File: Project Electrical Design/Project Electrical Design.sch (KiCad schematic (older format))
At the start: 2 parts

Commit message: Added Adafruit 8x8 Matrix to Kicad Project
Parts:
- added A?: Adafruit_8x8_Matrix, symbol CustomParts:Adafruit_8x8_Matrix
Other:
- moved on the sheet: A?
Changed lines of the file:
@@
 L CustomParts:MTK3339-GPS-Module A?
 U 1 1 5E668337
-P 4650 2650
-F 0 "A?" H 4300 3300 50  0000 C CNN
-F 1 "MTK3339-GPS-Module" H 4000 3400 50  0000 C CNN
-F 2 "" H 4000 3400 50  0001 C CNN
-F 3 "" H 4000 3400 50  0001 C CNN
-	1    4650 2650
+P 4300 2700
+F 0 "A?" H 3950 3250 50  0000 C CNN
+F 1 "MTK3339-GPS-Module" H 3550 3350 50  0000 C CNN
+F 2 "" H 3650 3450 50  0001 C CNN
+F 3 "" H 3650 3450 50  0001 C CNN
+	1    4300 2700
 	1    0    0    -1
 $EndComp
@@
 	1    0    0    -1
 $EndComp
+$Comp
+L CustomParts:Adafruit_8x8_Matrix A?
+U 1 1 5E66D79F
+P 6750 4500
+F 0 "A?" H 8178 4521 50  0000 L CNN
+F 1 "Adafruit_8x8_Matrix" H 8178 4430 50  0000 L CNN
+F 2 "" H 7650 5200 50  0001 C CNN
+F 3 "" H 7650 5200 50  0001 C CNN
+	1    6750 4500
+	1    0    0    -1
+$EndComp

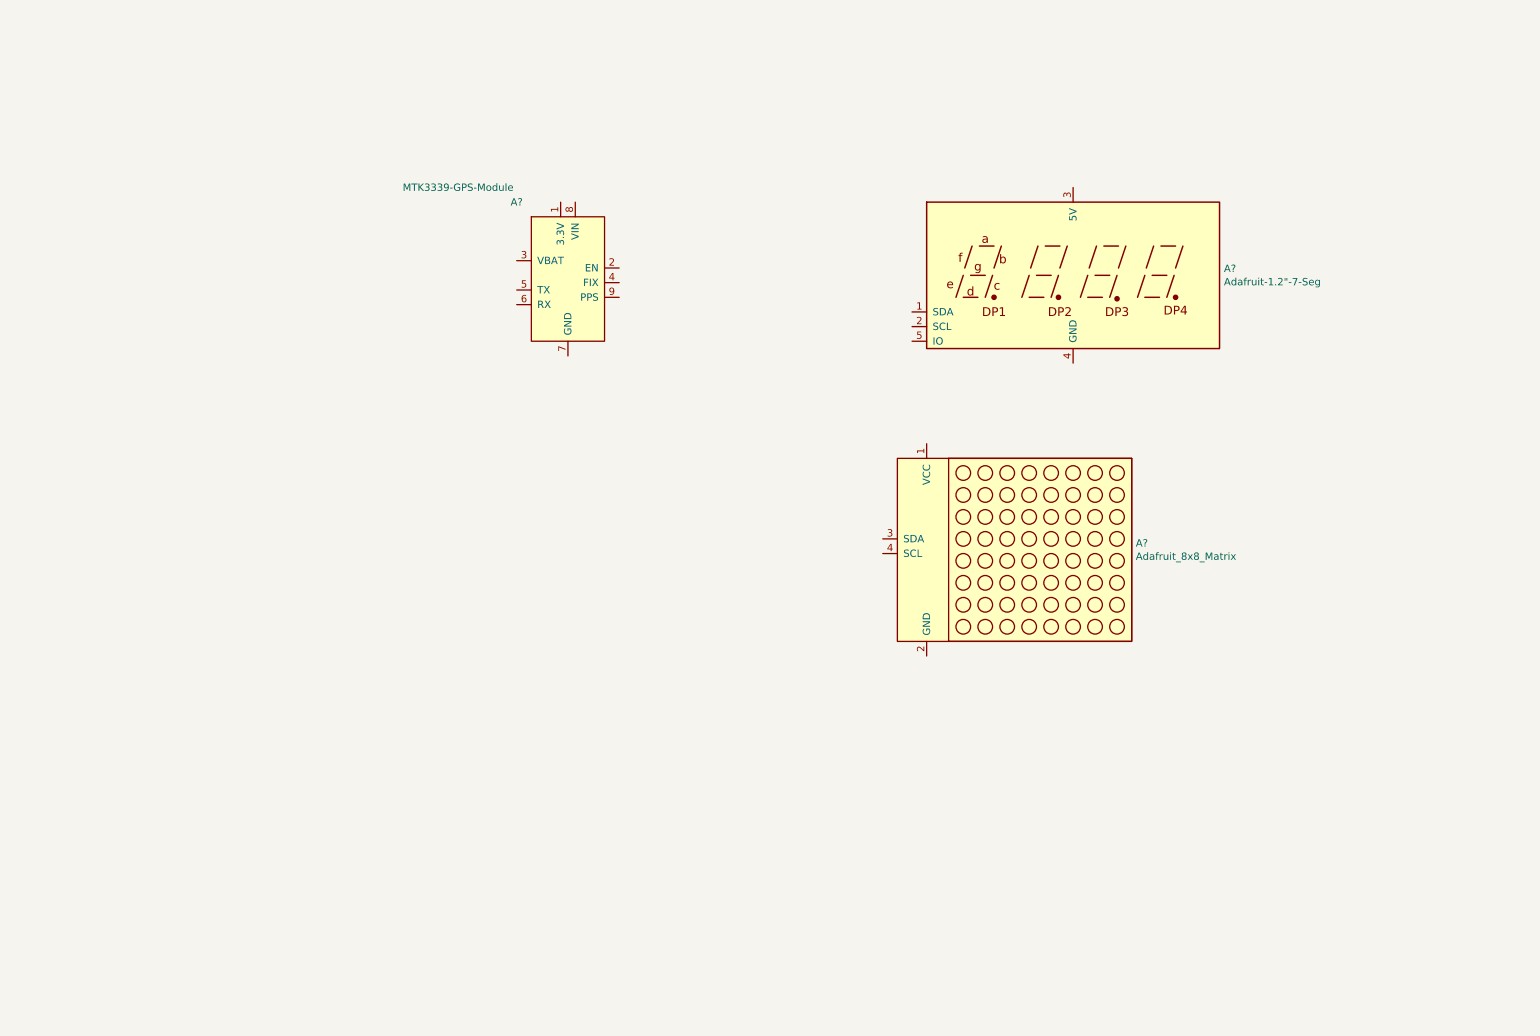
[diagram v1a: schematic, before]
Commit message: Created Component "From-Dragon-12-Board"
Please note that this component is not a complete description of the dragon 12 board.
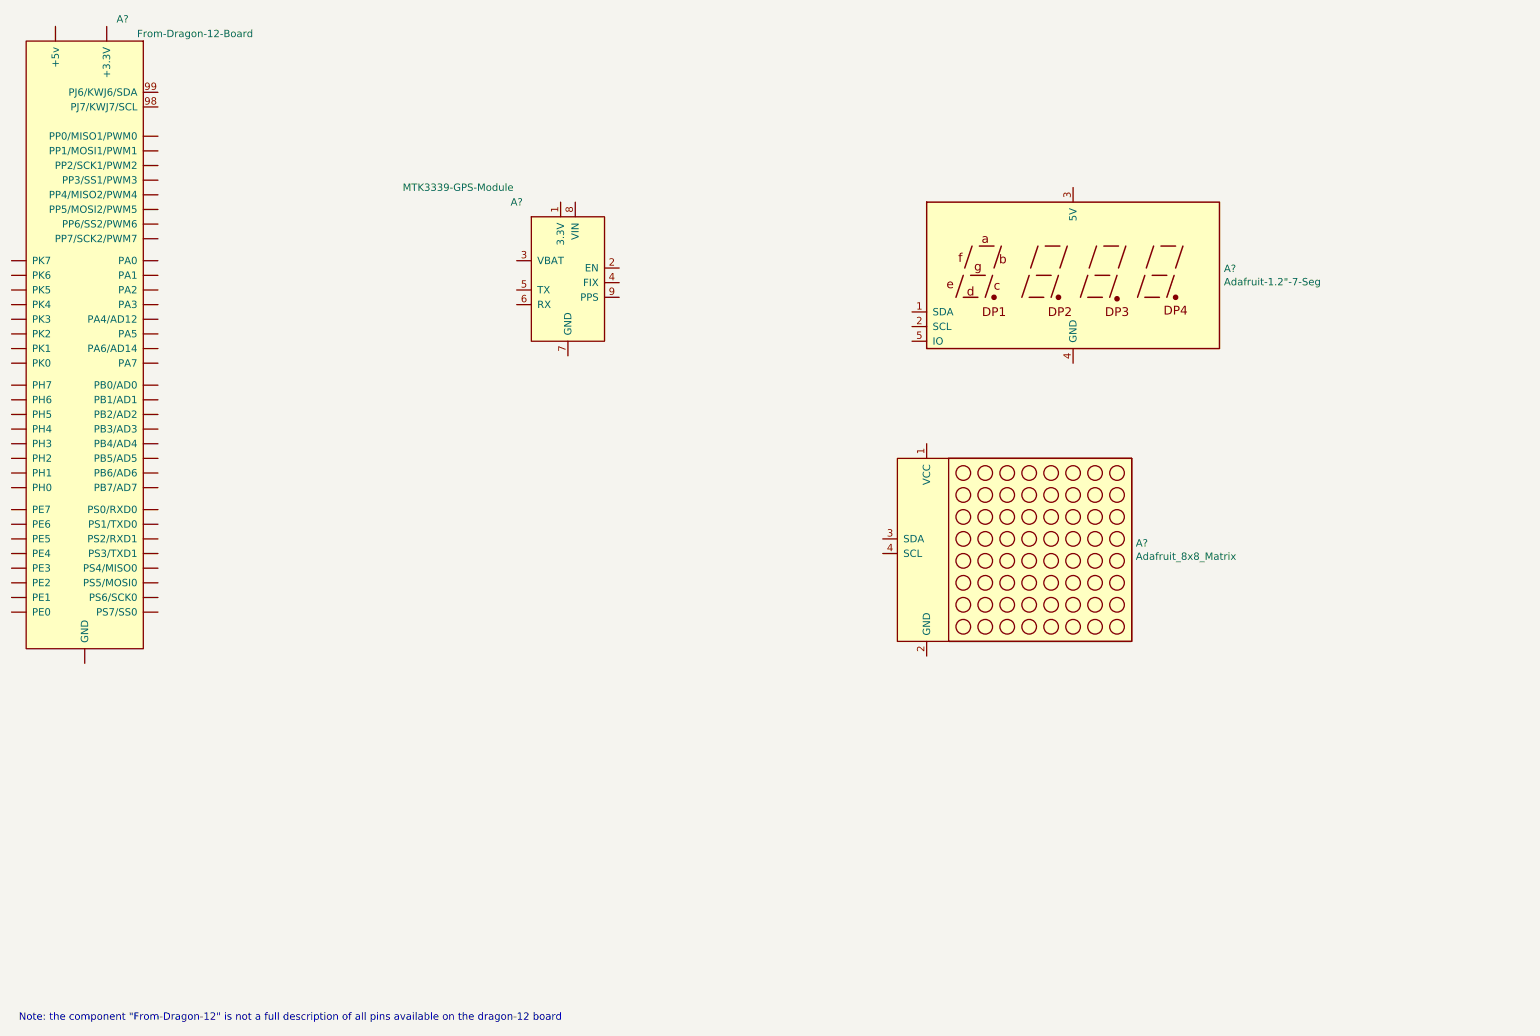
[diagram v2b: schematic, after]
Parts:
- added A?: From-Dragon-12-Board, symbol CustomParts:From-Dragon-12-Board
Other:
- note added: "Note: the component "From-Dragon-12" is not a full description of all pins available on the dragon-12 board\n"
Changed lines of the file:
@@
 	1    0    0    -1
 $EndComp
+$Comp
+L CustomParts:From-Dragon-12-Board A?
+U 1 1 5E677287
+P 1000 3850
+F 0 "A?" H 1300 6800 50  0000 R CNN
+F 1 "From-Dragon-12-Board" H 2150 6700 50  0000 R CNN
+F 2 "" H 600 6850 50  0001 C CNN
+F 3 "" H 600 6850 50  0001 C CNN
+	1    1000 3850
+	1    0    0    -1
+$EndComp
+Text Notes 550  7750 0    50   ~ 0
+Note: the component "From-Dragon-12" is not a full description of all pins available on the dragon-12 board\n
 $EndSCHEMATC

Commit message: Changes to dragon-12 board part, and basic connections to output display
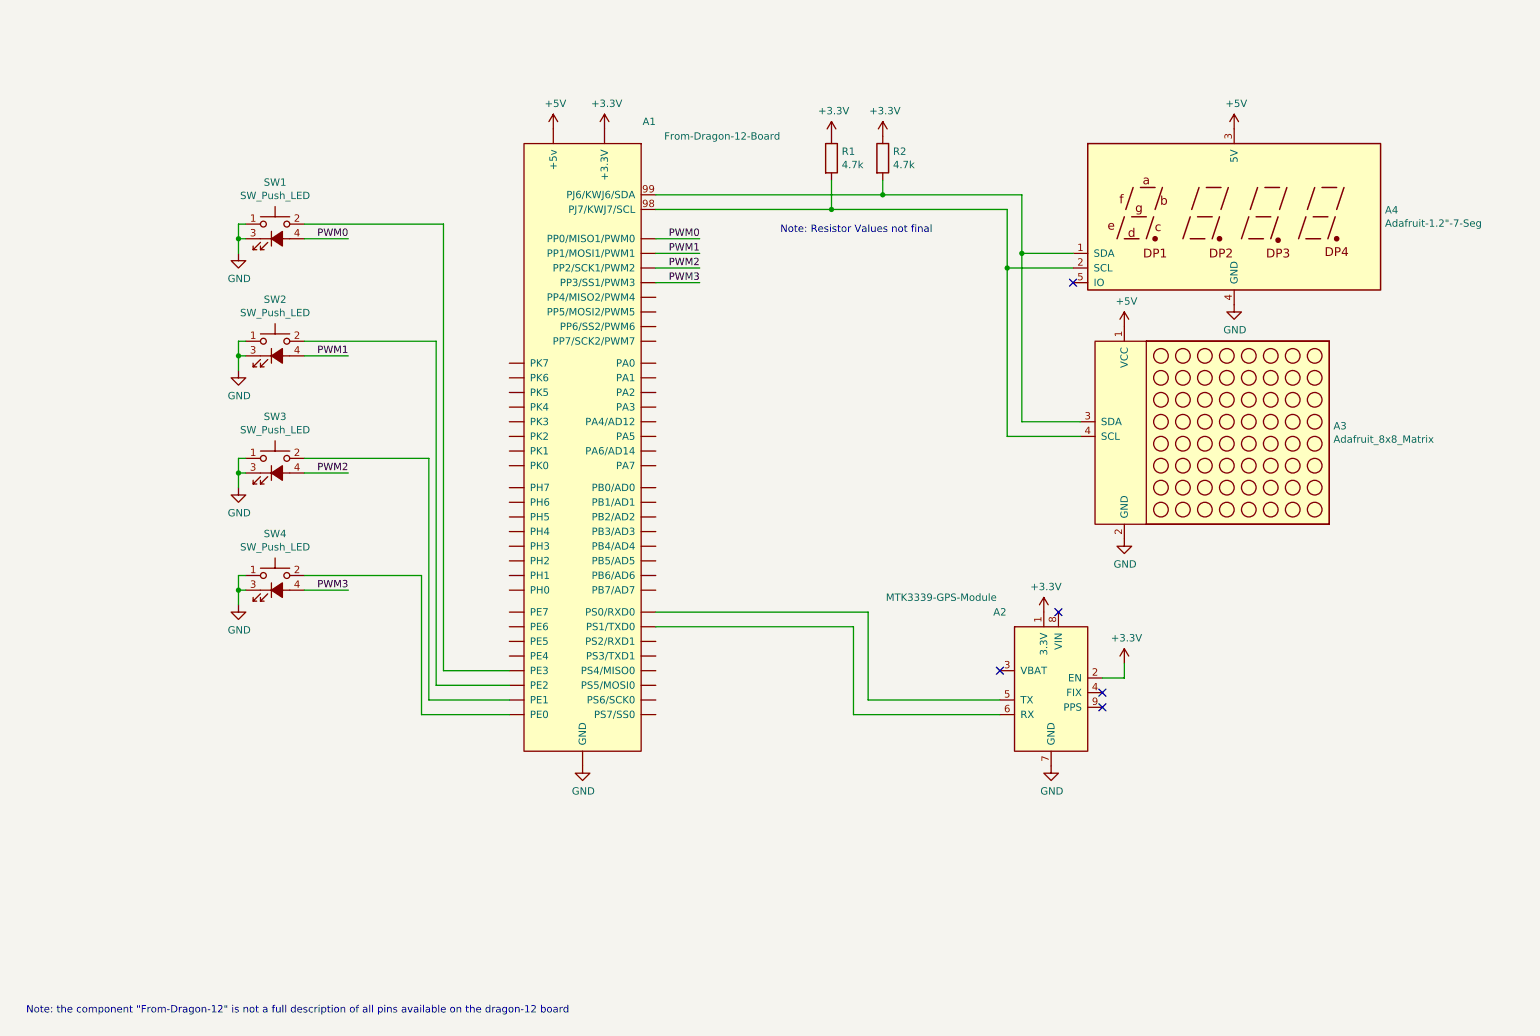
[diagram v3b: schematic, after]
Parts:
- added R1, R2: 4.7k, symbol Device:R
- added SW1, SW2, SW3, SW4: SW_Push_LED, symbol Switch:SW_Push_LED
- gave numbers to parts that had none: 4
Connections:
- net +3V3: now reaches A2.1 (3.3V)
- net +3V3: now also A1.~ (PS7/SS0), A2.2 (EN), R1.1, R2.1
- net at A2.5 (TX): now also A1.~ (PS7/SS0)
- net at A2.6 (RX): now also A1.~ (PS7/SS0)
- net GND: now reaches A2.7 (GND)
- net GND: now also A1.~ (PS7/SS0), A3.2 (GND), A4.4 (GND), SW1.1, SW1.3 (K), SW2.1, SW2.3 (K), SW3.1, SW3.3 (K), SW4.1, SW4.3 (K)
- net +5V: now reaches A3.1 (VCC)
- net +5V: now also A1.~ (PS7/SS0), A4.3 (5V)
- net at A3.3 (SDA): now also A1.99 (PJ6/KWJ6/SDA), A4.1 (SDA), R2.2
- net at A3.4 (SCL): now also A1.98 (PJ7/KWJ7/SCL), A4.2 (SCL), R1.2
- net PWM3: now reaches A1.~ (PS7/SS0)
- net PWM3: now also SW4.4 (A)
- new net: A1.~ (PS7/SS0), SW1.2
- new net: A1.~ (PS7/SS0), SW2.2
- new net: A1.~ (PS7/SS0), SW3.2
- new net: A1.~ (PS7/SS0), SW4.2
- new net PWM0: A1.~ (PS7/SS0), SW1.4 (A)
- new net PWM1: A1.~ (PS7/SS0), SW2.4 (A)
- new net PWM2: A1.~ (PS7/SS0), SW3.4 (A)
- no-connect marks 0 -> 5
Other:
- note added: "Note: Resistor Values not final\n\n"
- moved on the sheet: A1, A2, A3, A4

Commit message: Fixed Escheema config so CustomParts.lib is read relative to project path
(Should prevent all component loading issues)
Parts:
- removed A4: Adafruit-1.2\"-7-Seg, symbol Adafruit-1.2-7-seg:Adafruit-1.2"-7-Seg
- added A?: Adafruit-1.2\"-7-Seg, symbol CustomParts:Adafruit-1.2"-7-Seg
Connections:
- net +5V: now also A?.3 (5V)
- net GND: now also A?.4 (GND)
- net at A1.99 (PJ6/KWJ6/SDA), A3.3 (SDA), R2.2: now also A?.1 (SDA)
- net at A1.98 (PJ7/KWJ7/SCL), A3.4 (SCL), R1.2: now also A?.2 (SCL)
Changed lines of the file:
@@
-$EndComp
-$Comp
-L Adafruit-1.2-7-seg:Adafruit-1.2"-7-Seg A4
-U 1 1 5E66F4C1
-P 8850 2300
-F 0 "A4" H 9880 2396 50  0000 L CNN
-F 1 "Adafruit-1.2\"-7-Seg" H 9880 2305 50  0000 L CNN
-F 2 "" H 7950 3100 50  0001 C CNN
-F 3 "" H 7950 3100 50  0001 C CNN
-	1    8850 2300
-	1    0    0    -1
 $EndComp
 $Comp
@@
 	1    0    0    -1
 $EndComp
+$Comp
+L CustomParts:Adafruit-1.2"-7-Seg A?
+U 1 1 5E66C1F5
+P 8850 2300
+F 0 "A?" H 9880 2396 50  0000 L CNN
+F 1 "Adafruit-1.2\"-7-Seg" H 9880 2305 50  0000 L CNN
+F 2 "" H 7950 3100 50  0001 C CNN
+F 3 "" H 7950 3100 50  0001 C CNN
+	1    8850 2300
+	1    0    0    -1
+$EndComp

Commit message: Added pullups to buttons and current limiting resistors to LED backlights of buttons
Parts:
- added R10, R7, R8, R9: 10k, symbol Device:R
- added R3, R4, R5, R6: 220, symbol Device:R
- gave numbers to parts that had none: 1
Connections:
- net +3V3: no longer R1.1, R2.1
- net +5V: now also R1.1, R2.1, R10.1, R7.1, R8.1, R9.1; no longer A1.~ (PS7/SS0)
- net PWM0: now also R3.1; no longer SW1.4 (A)
- net PWM1: now also R4.1; no longer SW2.4 (A)
- net PWM2: now also R5.1; no longer SW3.4 (A)
- net PWM3: now also R6.1; no longer SW4.4 (A)
- net at A1.~ (PS7/SS0), SW1.2: now also R7.2
- net at A1.~ (PS7/SS0), SW2.2: now also R8.2
- net at A1.~ (PS7/SS0), SW3.2: now also R9.2
- net at A1.~ (PS7/SS0), SW4.2: now also R10.2
- new net: R3.2, SW1.4 (A)
- new net: R4.2, SW2.4 (A)
- new net: R5.2, SW3.4 (A)
- new net: R6.2, SW4.4 (A)
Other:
- moved on the sheet: SW1, SW2, SW3, SW4
